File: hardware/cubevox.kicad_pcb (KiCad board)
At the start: 4 copper layers, 200 x 150 mm, 223 parts, among them J1 USB-C, J101 J_IN NCJ6FA-H, J106 DC 9V, J108 OUT 6.35mm, J117 OLED SH1106, J3 TC2030-NL SWD, K101 G6K-2F-Y DC5, K102 G6K-2F-Y DC5, Q101 MMBT3904, SW101 ST-0-102 bat toggle, SW102 ST-0-102 bat toggle, SW103 ST-0-102 bat toggle, SW104 ST-0-102 bat toggle, SW105 ST-0-102 bat toggle, SW106 ST-0-102 bat toggle, SW107 ST-0-102 bat toggle, SW108 ST-0-102 bat toggle, U1 STM32H743VIT6, U101 CD74HC4067, U103 AP63205WU-7, U104 OPA2197IDR, U105 OPA2197IDR, U106 OPA2197IDR, U3 AP63203WU-7, U4 TLV75533PDBVR, U6 PCM5102APWR, U8 PCM1808PWR, Y1 25MHz 12pF

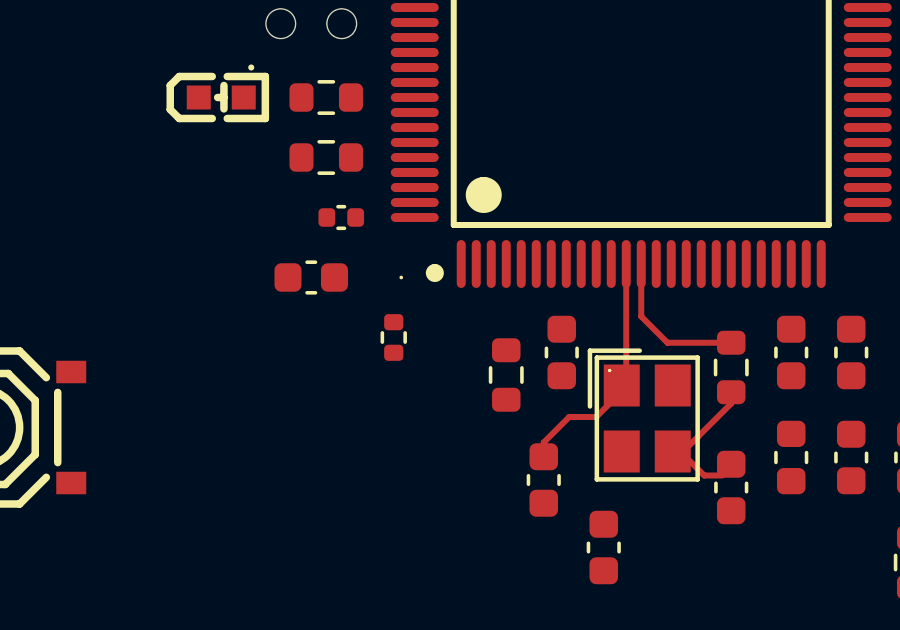
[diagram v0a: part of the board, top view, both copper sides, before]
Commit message: layout: change on /h7core_block/ADC_SCKI_SRC,/h7core_block/I2S_BCLK_SRC (ledger 0090)
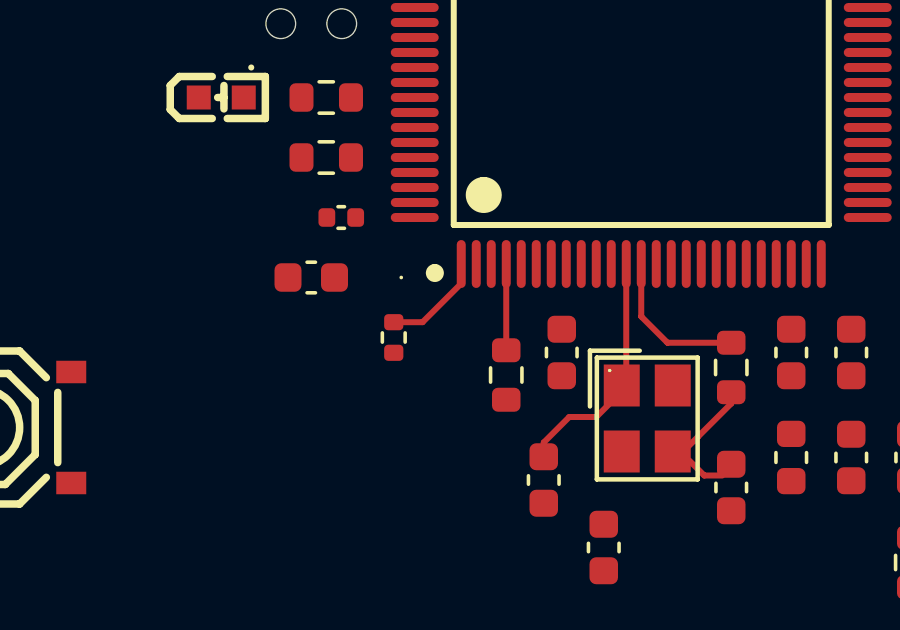
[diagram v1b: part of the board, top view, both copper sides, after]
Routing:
- net /h7core_block/ADC_SCKI_SRC: track 0.00 -> 2.78 mm
- net /h7core_block/I2S_BCLK_SRC: track 0.00 -> 2.10 mm
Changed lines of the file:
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@@
+	)
+	(segment
+		(start 90 92.2)
+		(end 88.71 93.49)
+		(width 0.2)
+		(layer "F.Cu")
+		(net "/h7core_block/ADC_SCKI_SRC")
+	)
+	(segment
+		(start 88.71 93.49)
+		(end 87.75 93.49)
+		(width 0.2)
+		(layer "F.Cu")
+		(net "/h7core_block/ADC_SCKI_SRC")
+	)
+	(segment
+		(start 91.5 92.2)
+		(end 91.5 94.3)
+		(width 0.2)
+		(layer "F.Cu")
+		(net "/h7core_block/I2S_BCLK_SRC")
 	)
 	(segment

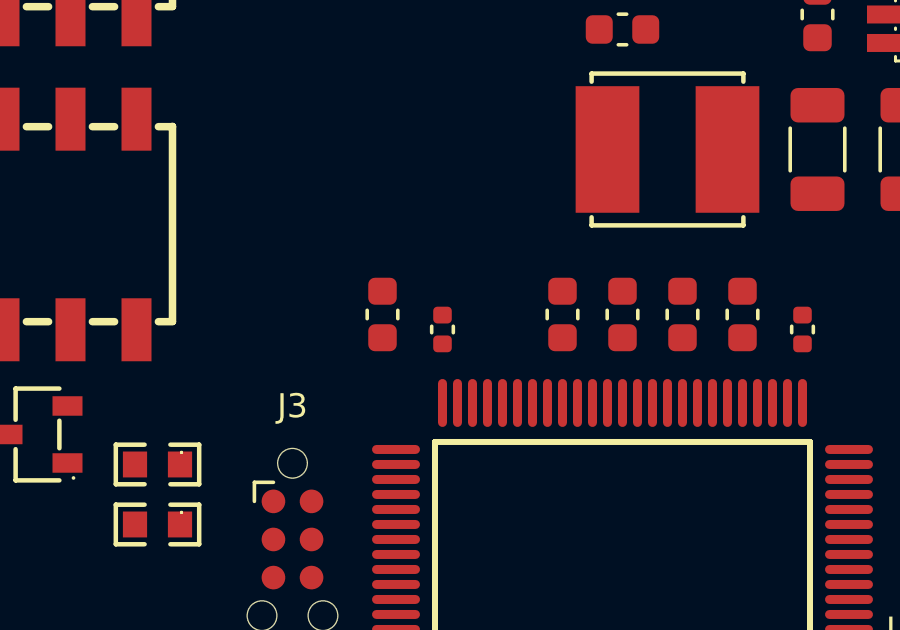
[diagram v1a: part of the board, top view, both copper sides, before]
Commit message: layout: move C1->86.50,73.50, C13->90.00,73.50, C57->88.25,74.00 (ledger 0091)
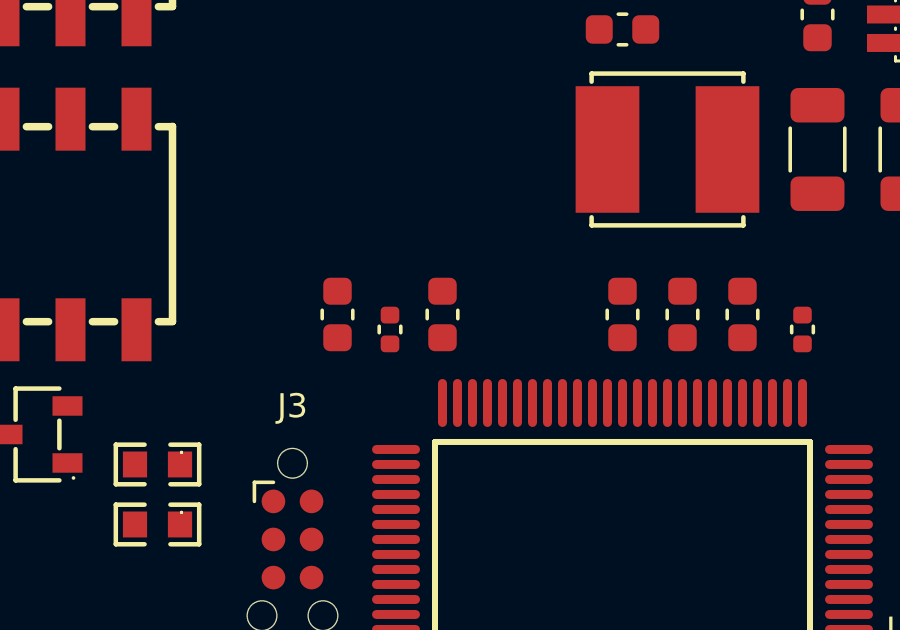
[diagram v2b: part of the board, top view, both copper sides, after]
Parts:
- moved C13 4.00 mm to (90.0, 73.5)
- moved C57 1.75 mm to (88.2, 74.0)
- moved C1 1.50 mm to (86.5, 73.5)
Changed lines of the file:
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@@
 	(footprint "Capacitor_SMD:C_0402_1005Metric"
 		(layer "F.Cu")
-		(at 90 74 90)
+		(at 88.25 74 90)
 		(descr "Capacitor SMD 0402 (1005 Metric), square (rectangular) end terminal, IPC-7351 nominal, (Body size source: IPC-SM-782 page 76, https://www.pcb-3d.com/wordpress/wp-content/uploads/ipc-sm-782a_amendment_1_and_2.pdf)")
 		(tags "capacitor")
@@
 	(footprint "Capacitor_SMD:C_0603_1608Metric"
 		(layer "F.Cu")
-		(at 94 73.5 90)
+		(at 90 73.5 90)
 		(descr "Capacitor SMD 0603 (1608 Metric), square (rectangular) end terminal, IPC-7351 nominal, (Body size source: IPC-SM-782 page 76, https://www.pcb-3d.com/wordpress/wp-content/uploads/ipc-sm-782a_amendment_1_and_2.pdf)")
 		(tags "capacitor")
@@
 	(footprint "Capacitor_SMD:C_0603_1608Metric"
 		(layer "F.Cu")
-		(at 88 73.5 90)
+		(at 86.5 73.5 90)
 		(descr "Capacitor SMD 0603 (1608 Metric), square (rectangular) end terminal, IPC-7351 nominal, (Body size source: IPC-SM-782 page 76, https://www.pcb-3d.com/wordpress/wp-content/uploads/ipc-sm-782a_amendment_1_and_2.pdf)")
 		(tags "capacitor")

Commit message: layout: change on /BUCK5_BST,/BUCK5_SW,/h7core_block/BUCK_BST,/h7core_block/BUCK_SW (ledger 0092)
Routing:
- net /h7core_block/BUCK_SW: track 0.00 -> 3.90 mm
- net /BUCK5_SW: track 0.00 -> 3.80 mm
- net /h7core_block/BUCK_BST: track 0.00 -> 1.83 mm
- net /BUCK5_BST: track 0.00 -> 1.70 mm
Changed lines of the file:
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@@
+	)
+	(segment
+		(start 93.05 50.25)
+		(end 92.8 50)
+		(width 0.2)
+		(layer "F.Cu")
+		(net "/BUCK5_BST")
+	)
+	(segment
+		(start 93.05 51.6)
+		(end 93.05 50.25)
+		(width 0.2)
+		(layer "F.Cu")
+		(net "/BUCK5_BST")
+	)
+	(segment
+		(start 94.1 51.6)
+		(end 94.1 47.8)
+		(width 0.5)
+		(layer "F.Cu")
+		(net "/BUCK5_SW")
 	)
 	(segment
@@
 		(net "/h7core_block/HSE_XTAL_OUT")
 	)
+	(segment
+		(start 95.5 62.3)
+		(end 95.5 66.2)
+		(width 0.5)
+		(layer "F.Cu")
+		(net "/h7core_block/BUCK_SW")
+	)
+	(segment
+		(start 96.45 62.3)
+		(end 96.45 63.675)
+		(width 0.2)
+		(layer "F.Cu")
+		(net "/h7core_block/BUCK_BST")
+	)
+	(segment
+		(start 96.45 63.675)
+		(end 96.775 64)
+		(width 0.2)
+		(layer "F.Cu")
+		(net "/h7core_block/BUCK_BST")
+	)
 	(embedded_fonts no)

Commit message: layout: change on /h7core_block/VCAP1,/h7core_block/VCAP2 (ledger 0093)
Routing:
- net /h7core_block/VCAP1: track 0.00 -> 2.10 mm
- net /h7core_block/VCAP2: track 0.00 -> 1.49 mm
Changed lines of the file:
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@@
+	)
+	(segment
+		(start 104.2 79)
+		(end 105.2 79)
+		(width 0.2)
+		(layer "F.Cu")
+		(net "/h7core_block/VCAP1")
+	)
+	(segment
+		(start 105.2 79)
+		(end 105.975 78.225)
+		(width 0.2)
+		(layer "F.Cu")
+		(net "/h7core_block/VCAP1")
+	)
+	(segment
+		(start 91 75.2)
+		(end 90.3 74.5)
+		(width 0.2)
+		(layer "F.Cu")
+		(net "/h7core_block/VCAP2")
+	)
+	(segment
+		(start 91 75.7)
+		(end 91 75.2)
+		(width 0.2)
+		(layer "F.Cu")
+		(net "/h7core_block/VCAP2")
 	)
 	(segment

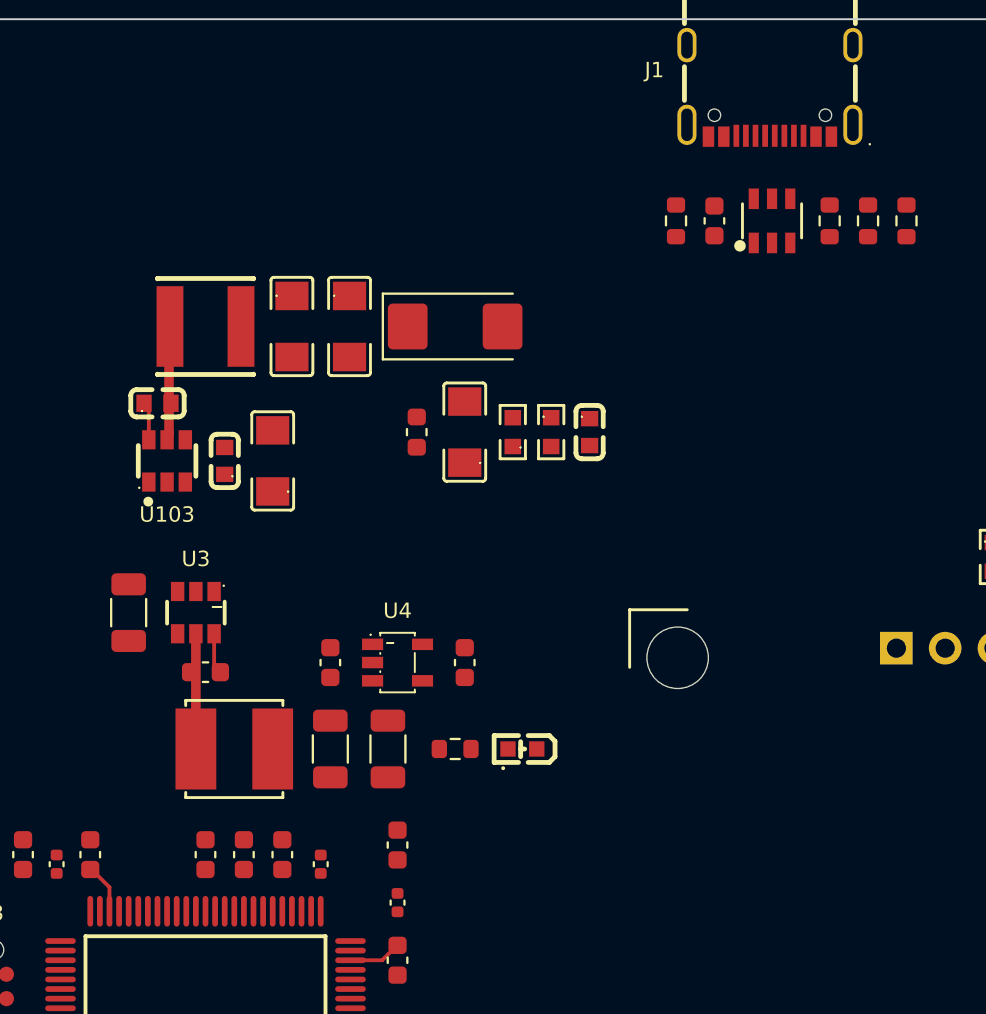
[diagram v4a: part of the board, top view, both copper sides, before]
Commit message: layout: change on /GND,/h7core_block/CC1,/h7core_block/CC2,/h7core_block/USB_DM,/h7core_block/USB_DP,/h7core_block/VBUS (ledger 0094)
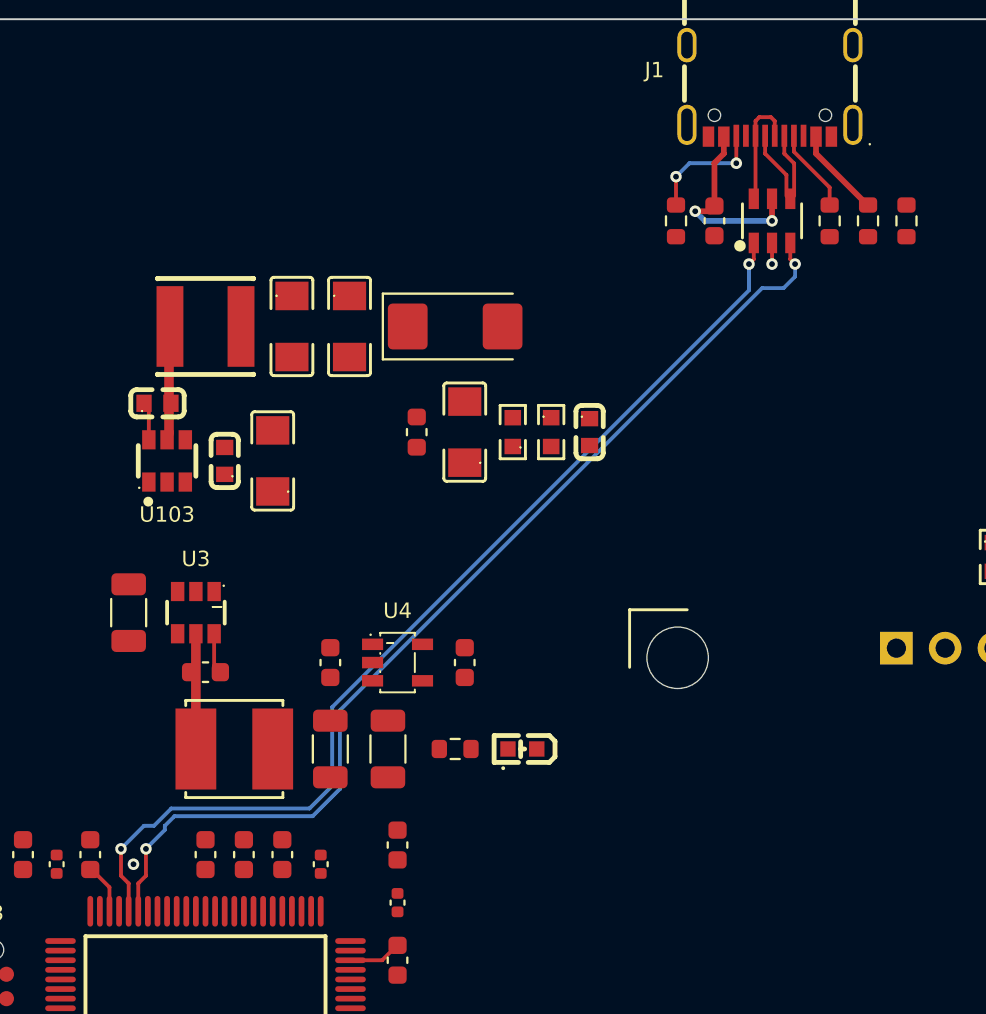
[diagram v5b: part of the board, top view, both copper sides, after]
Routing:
- net /h7core_block/USB_DM: track 0.00 -> 59.3 mm, vias 0 -> 2
- net /h7core_block/USB_DP: track 0.00 -> 57.2 mm, vias 0 -> 2
- net /h7core_block/VBUS: track 0.00 -> 14.4 mm, vias 0 -> 2
- net /h7core_block/CC2: track 0.00 -> 6.33 mm, vias 0 -> 2
- net /h7core_block/CC1: track 0.00 -> 4.38 mm
- net /GND: track 0.00 -> 1.10 mm, vias 0 -> 2

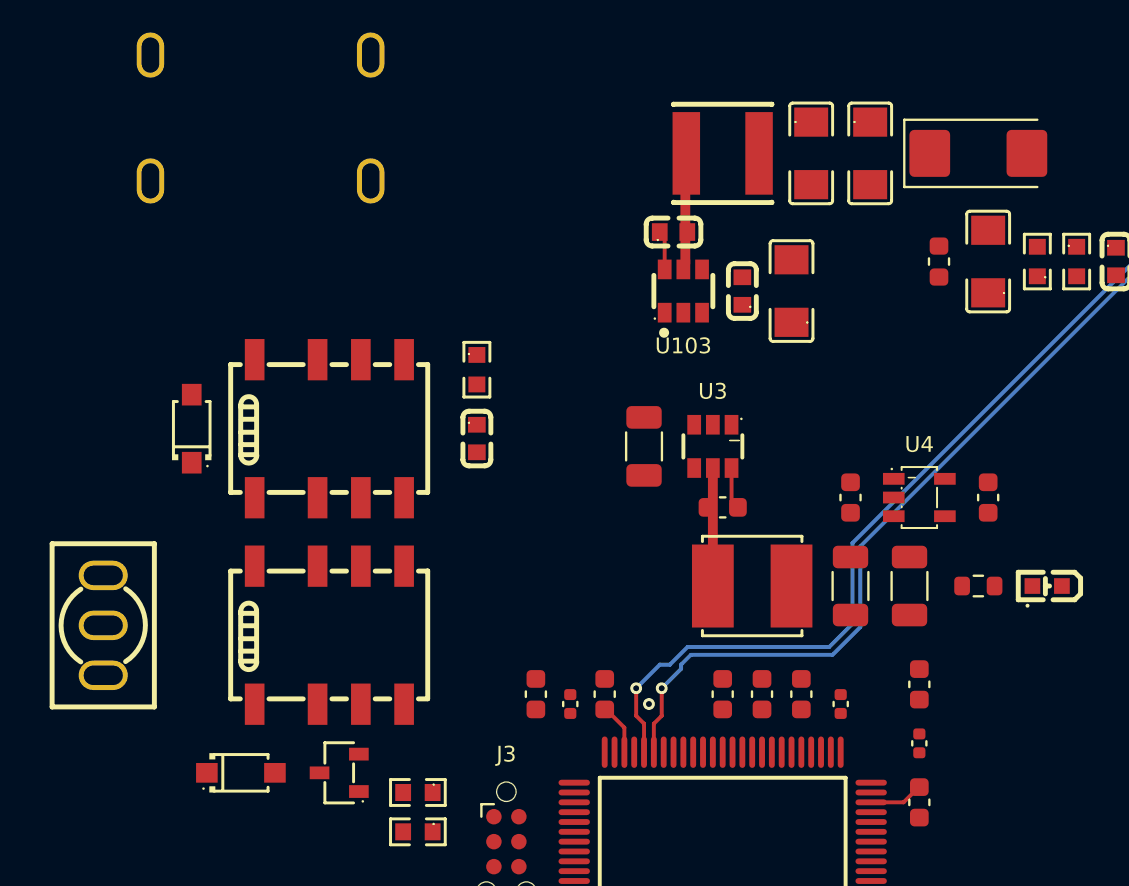
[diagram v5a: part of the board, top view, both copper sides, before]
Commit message: layout: change on /5V,/GND (ledger 0095)
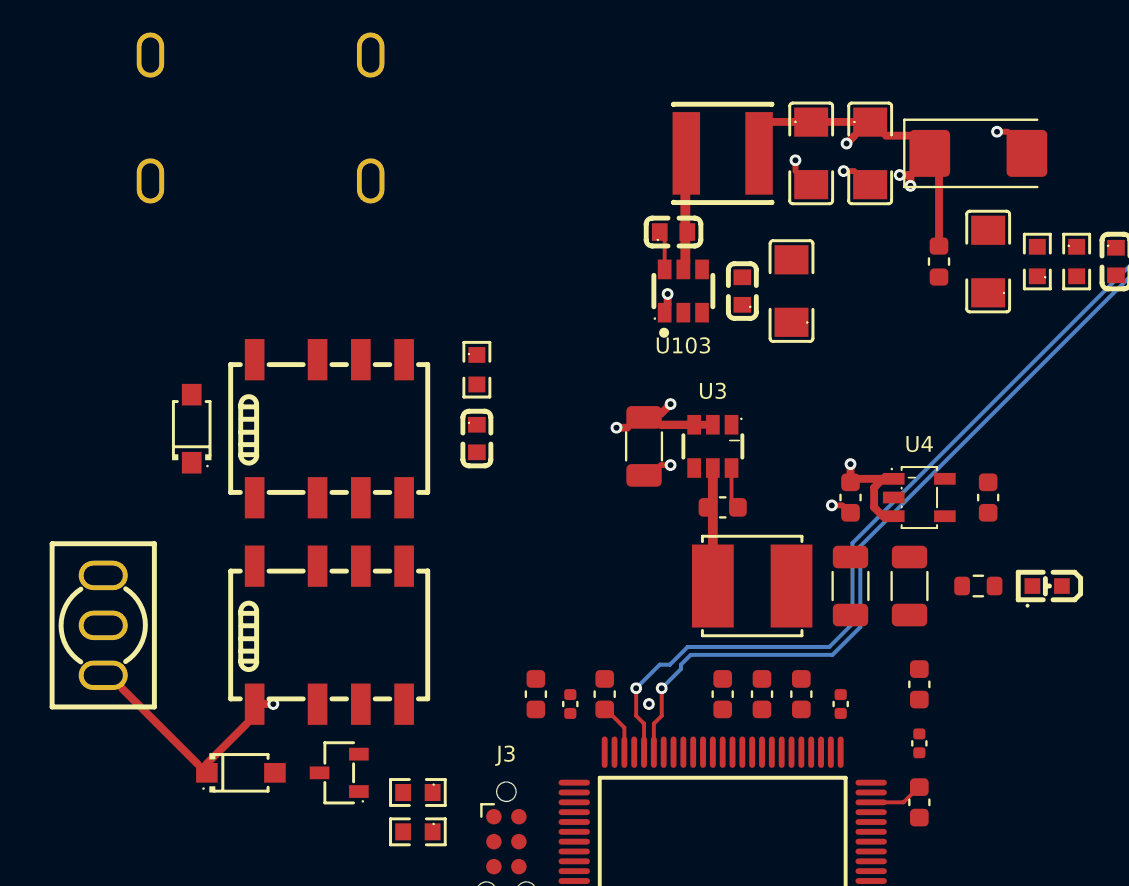
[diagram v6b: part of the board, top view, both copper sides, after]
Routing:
- net /5V: track 0.00 -> 94.8 mm, vias 0 -> 8
- net /GND: track 1.10 -> 3.80 mm, vias 2 -> 7
